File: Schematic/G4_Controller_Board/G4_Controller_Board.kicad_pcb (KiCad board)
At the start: 2 copper layers, 125.7 x 36.8 mm, 41 parts, among them J10 Solenoid, J11 Board Interconnect, J12 SolenoidTrig A (Optional), J13 SolenoidTrig B (Optional), J14 Board Interconnect, J17 IR LED Rec., J18 IR LED Emitter, J19 Positive BUS, J2 ESC Right, J20 Negative BUS, J3 ESC Left, J6 I2C Out, J7 Rev Trigger (Optional), J8 Fire Trigger, J9 Magazine Removal Trigger, Q1 2N7000, Q2 Q_NMOS_GDS, Q3 Q_PMOS_GDS, SW2 Preset A, SW3 Preset B, SW4 Preset C, SW7 RotaryEncoder_Switch, U1 ESP32-LOLIN32-Lite, U2 Mini360

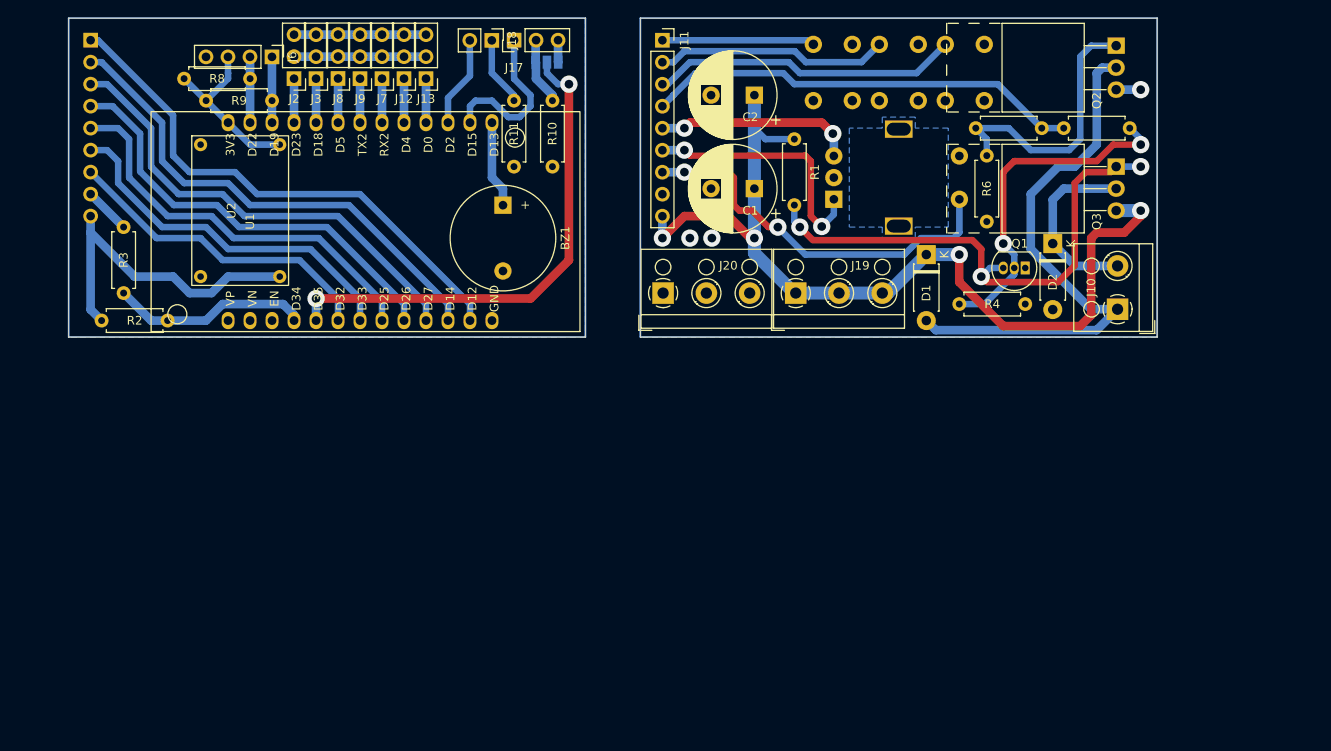
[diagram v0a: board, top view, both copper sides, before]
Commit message: update PCB
trying 3 PCB config (floating buttons, ESP32, and fast decay driver)
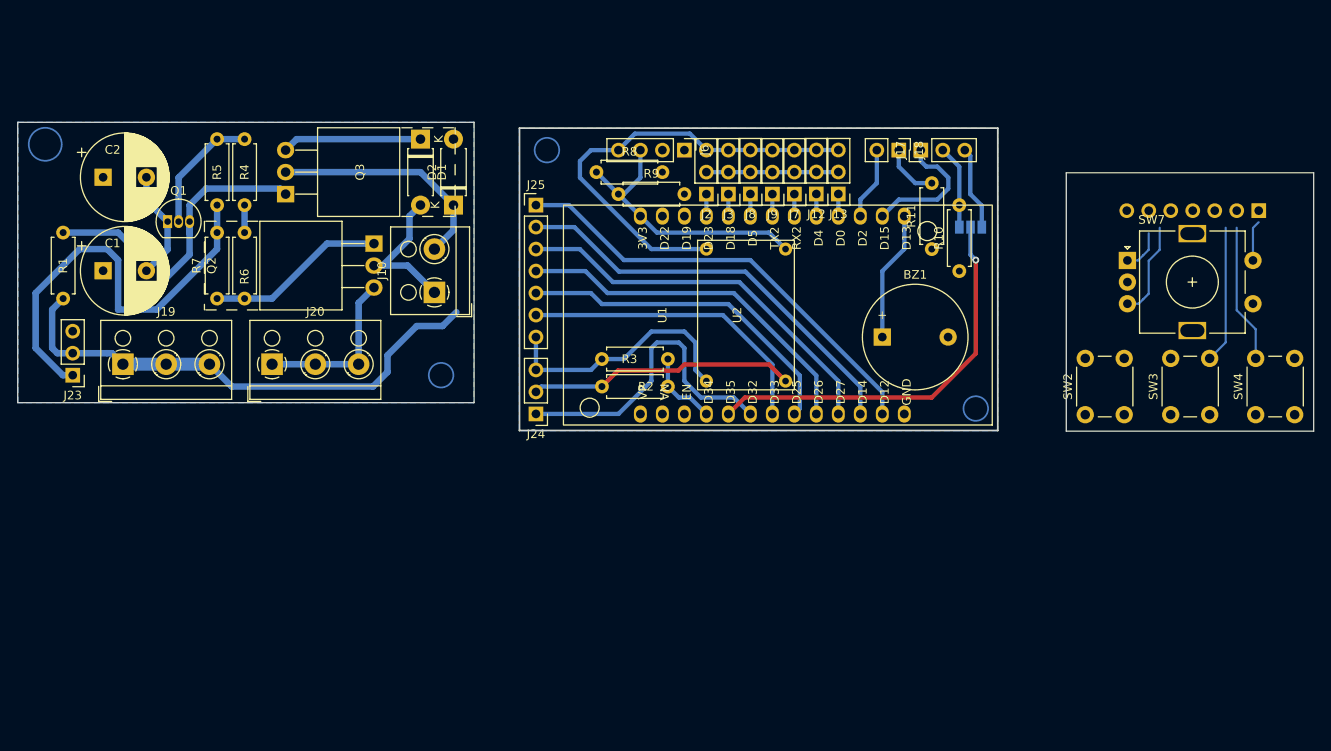
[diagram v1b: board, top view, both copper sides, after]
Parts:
- removed J11: Board Interconnect, Connector_PinSocket_2.54mm:PinSocket_1x09_P2.54mm_Vertical
- removed J14: Board Interconnect, Connector_PinHeader_2.54mm:PinHeader_1x09_P2.54mm_Vertical
- added J23: Board Interconnect, Connector_PinHeader_2.54mm:PinHeader_1x03_P2.54mm_Vertical, F.Cu at (55.1, 111.1)
- added J24: Board Interconnect, Connector_PinHeader_2.54mm:PinHeader_1x03_P2.54mm_Vertical, F.Cu at (108.6, 115.6)
- added J25: Board Interconnect, Connector_PinHeader_2.54mm:PinHeader_1x07_P2.54mm_Vertical, F.Cu at (108.6, 91.4)
- added J26: Board Interconnect, Connector_PinHeader_2.54mm:PinHeader_1x07_P2.54mm_Horizontal, B.Cu at (192.1, 92.1)
- SW2, SW3, SW4, SW7: moved to F.Cu
- moved R5 105.4 mm to (71.8, 83.8), turned to -90 degrees
- moved Q1 99.2 mm to (66.0, 93.3), turned to 0 degrees
- moved Q3 96.0 mm to (79.7, 90.2), turned to 90 degrees
- moved R4 90.9 mm to (74.9, 91.4), turned to 90 degrees
- moved R7 89.8 mm to (71.8, 102.2), turned to 90 degrees
- moved Q2 88.7 mm to (89.9, 95.9)
- moved R1 86.4 mm to (54.0, 102.2), turned to 90 degrees
- moved R6 85.7 mm to (74.9, 94.6), turned to -90 degrees
- moved J10 78.9 mm to (96.9, 101.5)
- moved J19 78.1 mm to (60.9, 109.8)
- moved C1 75.8 mm to (58.6, 99.0), turned to 0 degrees
- moved C2 75.8 mm to (58.6, 88.2), turned to 0 degrees
- moved D2 69.4 mm to (99.1, 91.4), turned to 90 degrees
- moved SW4 66.6 mm to (191.7, 115.6), turned to 90 degrees
- moved D1 59.9 mm to (95.2, 83.8)
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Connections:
- SW7 pad MP: Tab -> (no net)
- U1 pad 12: /Encoder Switch -> /Pusher Pin
- U1 pad 13: /Encoder A -> /Encoder Switch
- U1 pad 14: /Encoder B -> /Encoder A
- U1 pad 15: /Pusher Pin -> /Encoder B
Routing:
- net GND: track 38.7 -> 148.1 mm, vias 3 -> 0
- net /SOLENOID_A: track 63.6 -> 18.1 mm
- net /Preset A: track 89.4 -> 45.0 mm
- net /Encoder Switch: track 82.8 -> 40.1 mm, vias 2 -> 0
- net +12V: track 144.4 -> 106.5 mm, vias 4 -> 0
- net /Preset B: track 84.3 -> 48.3 mm
- net /Encoder A: track 71.7 -> 44.0 mm, vias 2 -> 0
- net /High Side Driver: track 39.7 -> 14.5 mm, vias 2 -> 0
- net Net-(Q1-D): track 60.7 -> 41.6 mm, vias 3 -> 0
- net /Encoder B: track 69.8 -> 52.9 mm, vias 2 -> 0
- net /Pusher Pin: track 100.7 -> 85.3 mm
- net /Battery Reader: track 23.0 -> 8.94 mm
- net /IR Reciever: track 58.2 -> 46.3 mm, vias 2 -> 1
- net +3V3: track 20.3 -> 32.0 mm
- net /Preset C: track 78.7 -> 67.5 mm
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- removed copper zone on B.Cu, net Tab
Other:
- board size 125.7 x 36.8 mm -> 149.7 x 35.7 mm

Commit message: update PCB traces
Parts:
- moved R1 37.7 mm to (84.5, 80.0)
- moved Q1 17.4 mm to (68.9, 76.2), turned to -90 degrees
- moved J24 5.05 mm to (108.6, 110.5), turned to 0 degrees
- moved D1 3.81 mm to (99.1, 83.8)
- moved D2 3.81 mm to (95.2, 91.4)
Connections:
- J25 pad 1: /Preset C -> /Encoder Switch
- J25 pad 4: /Encoder B -> /Preset C
- J25 pad 5: /Encoder A -> /Encoder B
- J25 pad 6: /Encoder Switch -> /Encoder A
- J26 pad 1: /Preset C -> /Encoder Switch
- J26 pad 4: /Encoder B -> /Preset C
- J26 pad 5: /Encoder A -> /Encoder B
- J26 pad 6: /Encoder Switch -> /Encoder A
- SW2 pad 1: /Preset A -> GND
- SW2 pad 2: GND -> /Preset A
- U1 pad 13: /Encoder Switch -> /Encoder A
- U1 pad 14: /Encoder A -> /Encoder B
- U1 pad 15: /Encoder B -> /Preset B
- U1 pad 17: /Preset B -> /Preset C
- U1 pad 18: /Preset C -> /Encoder Switch
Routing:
- net /Preset A: track 45.0 -> 109.5 mm
- net Net-(Q1-D): track 41.6 -> 0.00 mm
- net /Preset B: track 48.3 -> 22.8 mm
- net GND: track 148.1 -> 129.3 mm
- net +12V: track 106.5 -> 125.1 mm
- net /Encoder Switch: track 40.1 -> 57.5 mm
- net /Preset C: track 67.5 -> 80.0 mm
- net /High Side Driver: track 14.5 -> 3.18 mm
- net /SOLENOID_B: track 27.0 -> 22.9 mm
- net /SOLENOID_A: track 18.1 -> 20.8 mm
- net /Pusher Pin: track 85.3 -> 87.6 mm
- net /Encoder A: track 44.0 -> 43.0 mm
- net /Encoder B: track 52.9 -> 52.0 mm

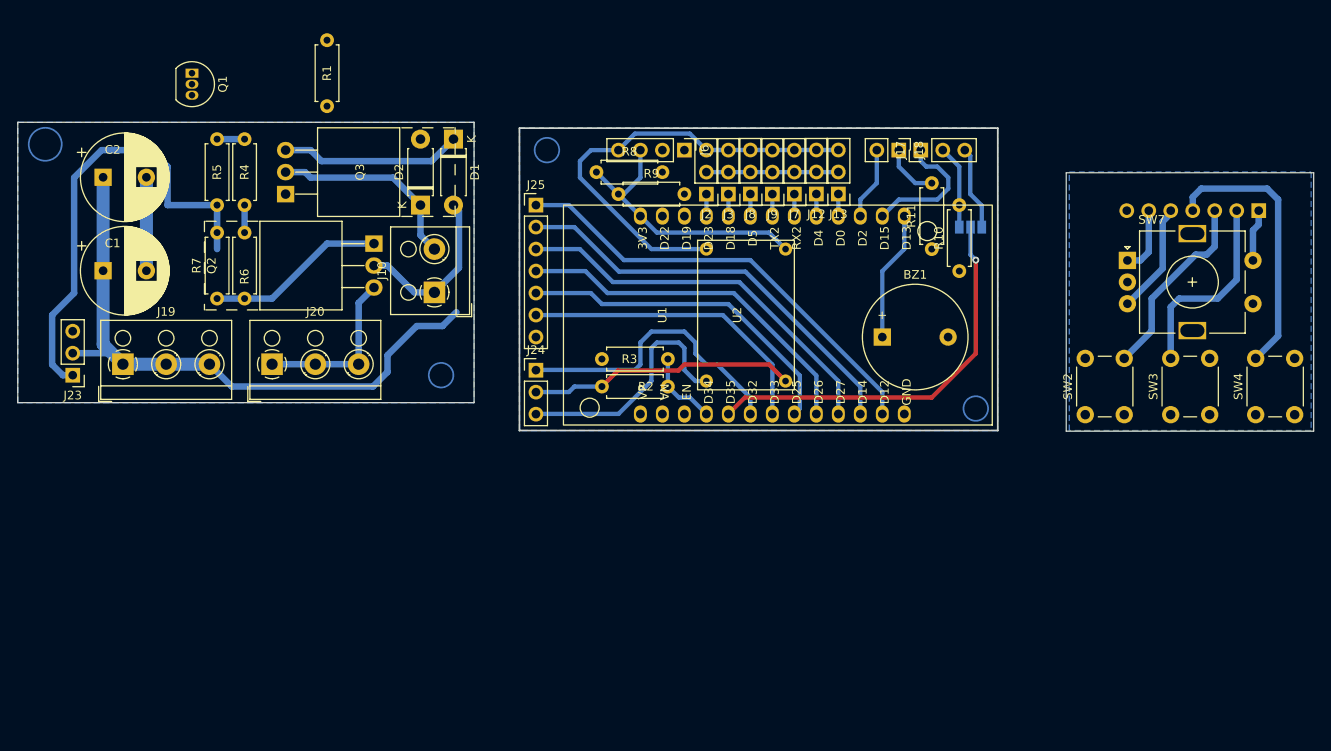
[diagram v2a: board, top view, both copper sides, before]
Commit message: create machine code for PCB
nc code generated to machine out the physical PCB tests
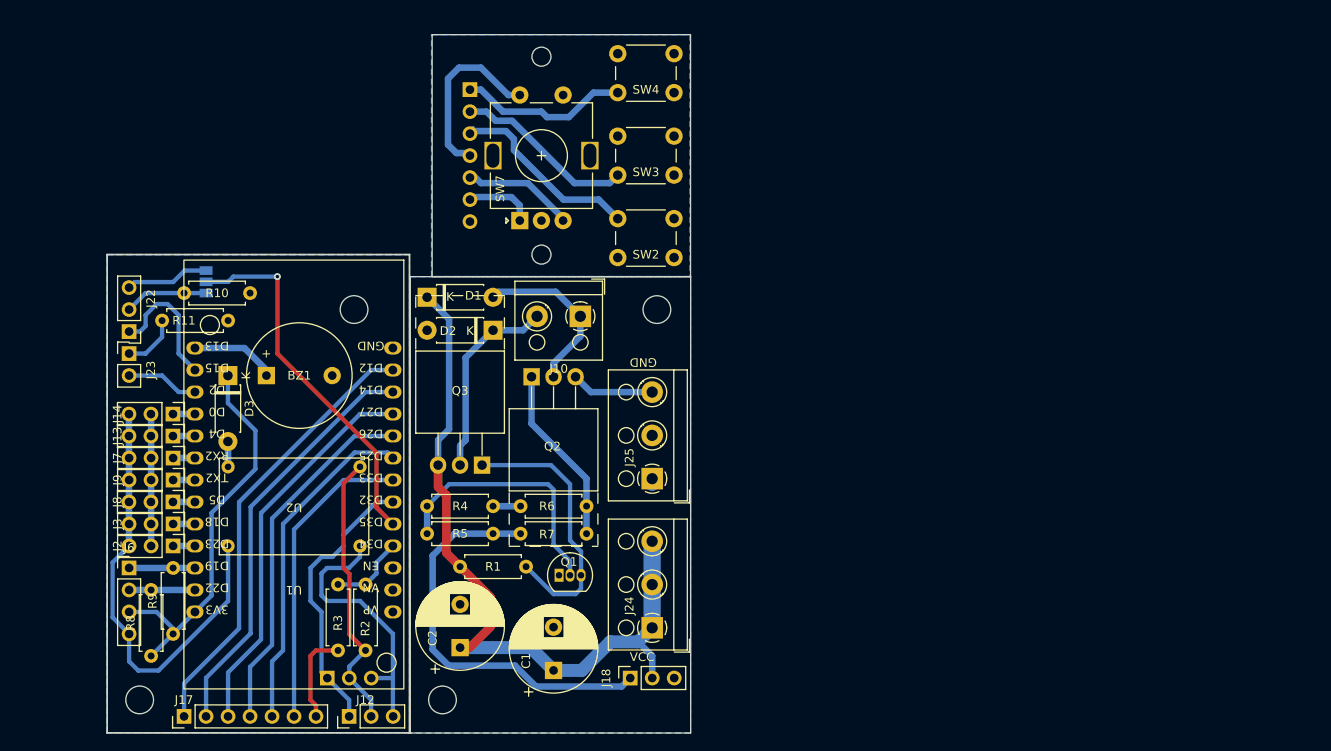
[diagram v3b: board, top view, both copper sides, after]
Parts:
- added D3: 1N4001, Diode_THT:D_DO-41_SOD81_P7.62mm_Horizontal, F.Cu at (73.0, 111.1)
- added H1: MountingHole, MountingHole:MountingHole_3.2mm_M3, F.Cu at (87.6, 103.5)
- added H1: MountingHole, MountingHole:MountingHole_3.2mm_M3, F.Cu at (97.8, 148.6)
- added H1: MountingHole, MountingHole:MountingHole_3.2mm_M3, F.Cu at (62.8, 148.6)
- added H1: MountingHole, MountingHole:MountingHole_3.2mm_M3, F.Cu at (122.6, 103.5)
- added H1: MountingHole, MountingHole:MountingHole_2.2mm_M2, F.Cu at (109.2, 97.2)
- added H1: MountingHole, MountingHole:MountingHole_2.2mm_M2, F.Cu at (109.2, 74.3)
- added J16: Board Interconnect, Connector_PinHeader_2.54mm:PinHeader_1x03_P2.54mm_Vertical, B.Cu at (84.5, 146.1)
- added kibuzzard-65468392: G***, kibuzzard-65468392, B.Cu at (83.2, 122.6)
- added kibuzzard-654684EA: G***, kibuzzard-654684EA, B.Cu at (121.5, 135.3)
- added kibuzzard-654685C2: G***, kibuzzard-654685C2, B.Cu at (97.2, 113.6)
- added kibuzzard-654685F2: G***, kibuzzard-654685F2, B.Cu at (121.6, 84.5)
- J18: renamed from J23; footprint Connector_PinHeader_2.54mm:PinHeader_1x03_P2.54mm_Vertical -> Connector_PinSocket_2.54mm:PinSocket_1x03_P2.54mm_Vertical
- moved J22 93.8 mm to (61.6, 106.0), turned to 180 degrees
- moved J15 92.2 mm to (101.0, 78.1), turned to 180 degrees
- moved J23 92.0 mm to (61.6, 108.6), turned to 0 degrees
- moved JP1 88.5 mm to (70.5, 100.3), turned to 90 degrees
- moved R10 82.0 mm to (75.6, 101.6), turned to 180 degrees
- moved R11 81.7 mm to (73.0, 104.8), turned to 180 degrees
- moved J14 80.9 mm to (66.7, 115.6), turned to -90 degrees
- moved J6 80.3 mm to (61.6, 133.3), turned to 0 degrees
- moved J13 79.4 mm to (66.7, 118.1), turned to -90 degrees
- moved J7 78.0 mm to (66.7, 120.7), turned to -90 degrees
- moved SW4 76.8 mm to (124.5, 78.5), turned to 180 degrees
- moved J9 76.7 mm to (66.7, 123.2), turned to -90 degrees
- moved R8 75.9 mm to (64.1, 143.5), turned to 90 degrees
- moved J8 75.6 mm to (66.7, 125.7), turned to -90 degrees
- moved J3 74.6 mm to (66.7, 128.3), turned to -90 degrees
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- renumbered J24 to J12, J12 to J13, J13 to J14, J26 to J15, J25 to J17, J17 to J22, J18 to J23, J19 to J24, J20 to J25
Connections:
- J15 pad 1: /Encoder Switch -> /Preset C
- J15 pad 4: /Preset C -> /Encoder Switch
- J17 pad 1: /Encoder Switch -> /Preset C
- J17 pad 4: /Preset C -> /Encoder Switch
- U1 pad 15: /Preset B -> /Encoder Switch
- U1 pad 17: /Preset C -> /Preset B
- U1 pad 18: /Encoder Switch -> /Preset C
- U2 pad 4: +3V3 -> Net-(D3-A)
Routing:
- net /Preset B: track 22.8 -> 69.1 mm
- net /Preset A: track 109.5 -> 67.5 mm
- net Net-(Q1-D): track 0.00 -> 31.6 mm
- net /High Side Driver: track 3.18 -> 29.8 mm
- net +3V3: track 32.0 -> 45.2 mm
- net /Preset C: track 80.0 -> 71.0 mm
- net /Pusher Pin: track 87.6 -> 79.5 mm
- net /SCL/SCK (Clock): track 0.01 -> 7.62 mm
- net /SDA/SDI (Data): track 0.01 -> 7.62 mm
- net GND: track 129.3 -> 122.3 mm
- net +12V: track 125.1 -> 118.7 mm
- net /Buzzer: track 15.0 -> 9.94 mm
- net /Encoder Switch: track 57.5 -> 62.5 mm
- net /IR Reciever: track 46.3 -> 42.6 mm
- net Net-(D3-A): track 0.00 -> 2.92 mm
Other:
- board size 149.7 x 35.7 mm -> 67.4 x 80.7 mm
- board text added: "GND"
- board text added: "VCC"
